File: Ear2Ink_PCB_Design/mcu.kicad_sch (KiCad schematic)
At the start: 44 parts, among them J1 Conn_02x16_Top_Bottom, J2 Conn_01x08_Pin, J3 Conn_01x08_Pin, J4 Micro_SD_Card_Det1, J5 Conn_01x06_Pin, J6 Conn_01x04_Pin, J7 Conn_01x03_Pin, SW1 SW_Push, U1 STM32F411RETx, Y1 MAX7375AXR805

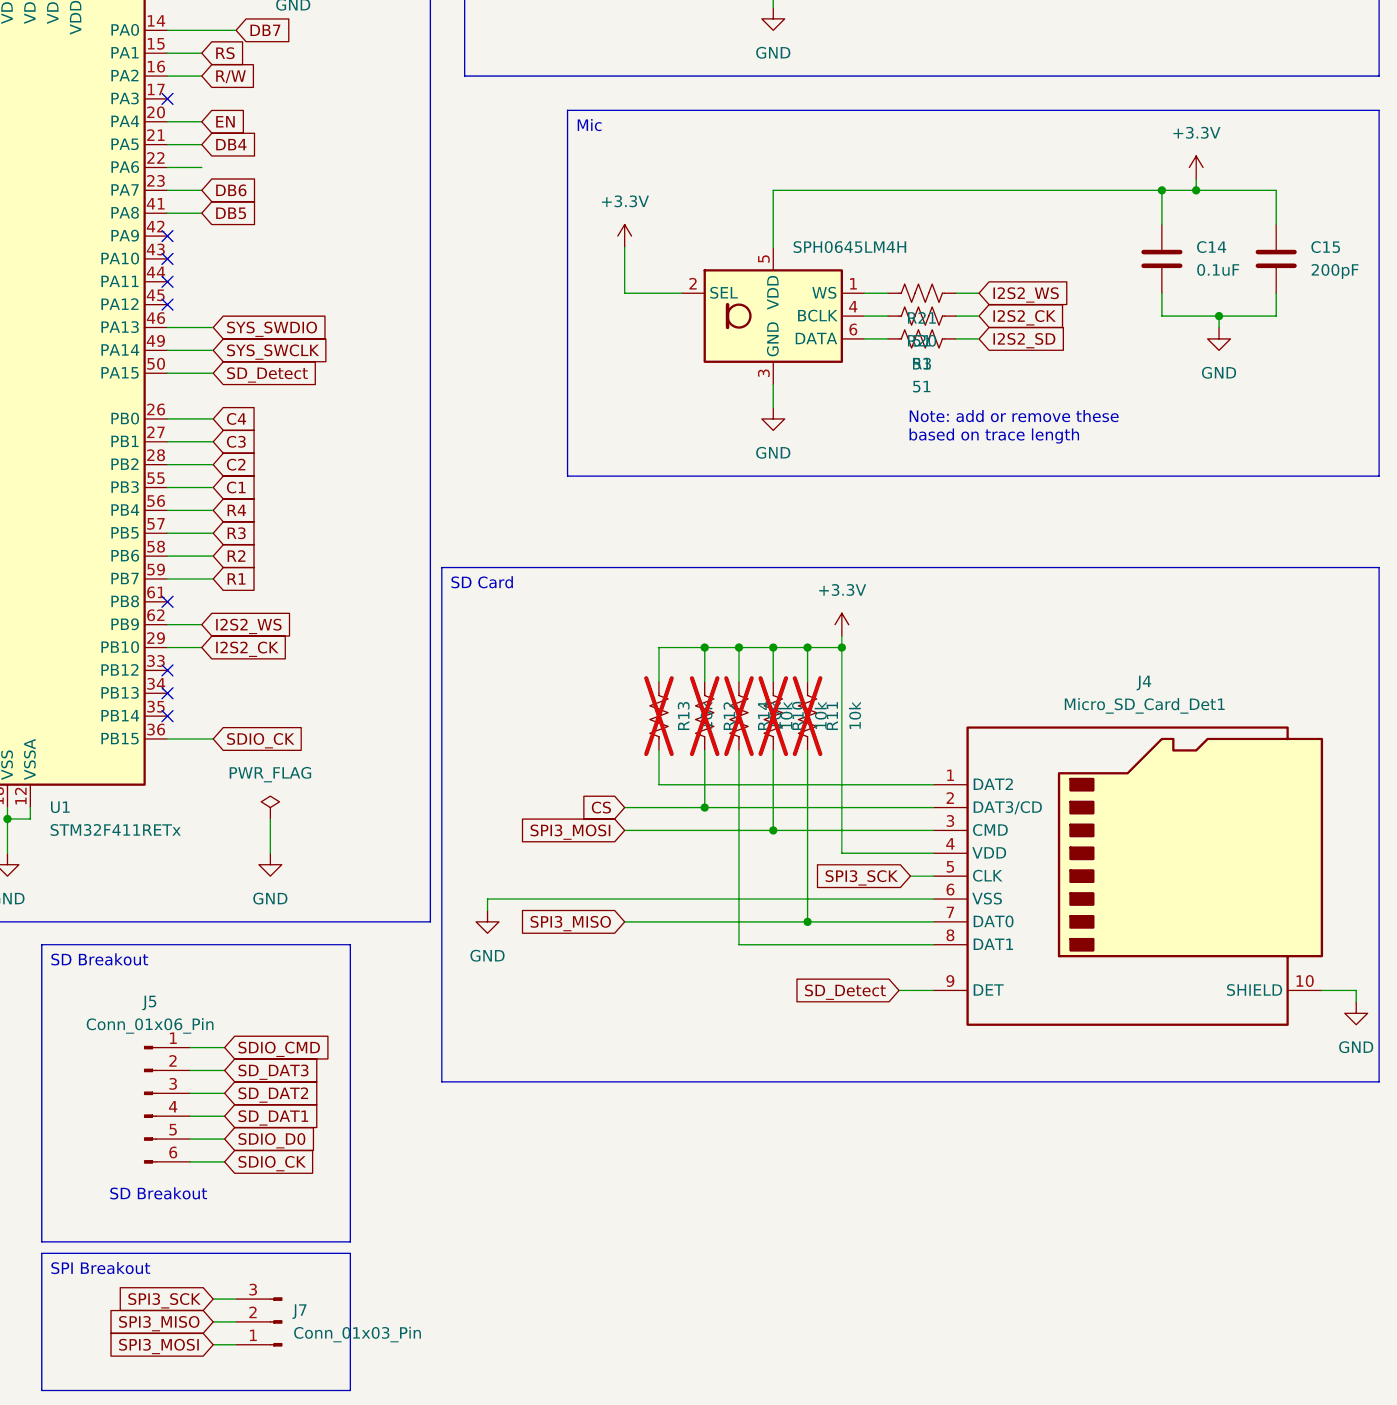
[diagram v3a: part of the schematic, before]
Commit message: fixed footprint issue with SD
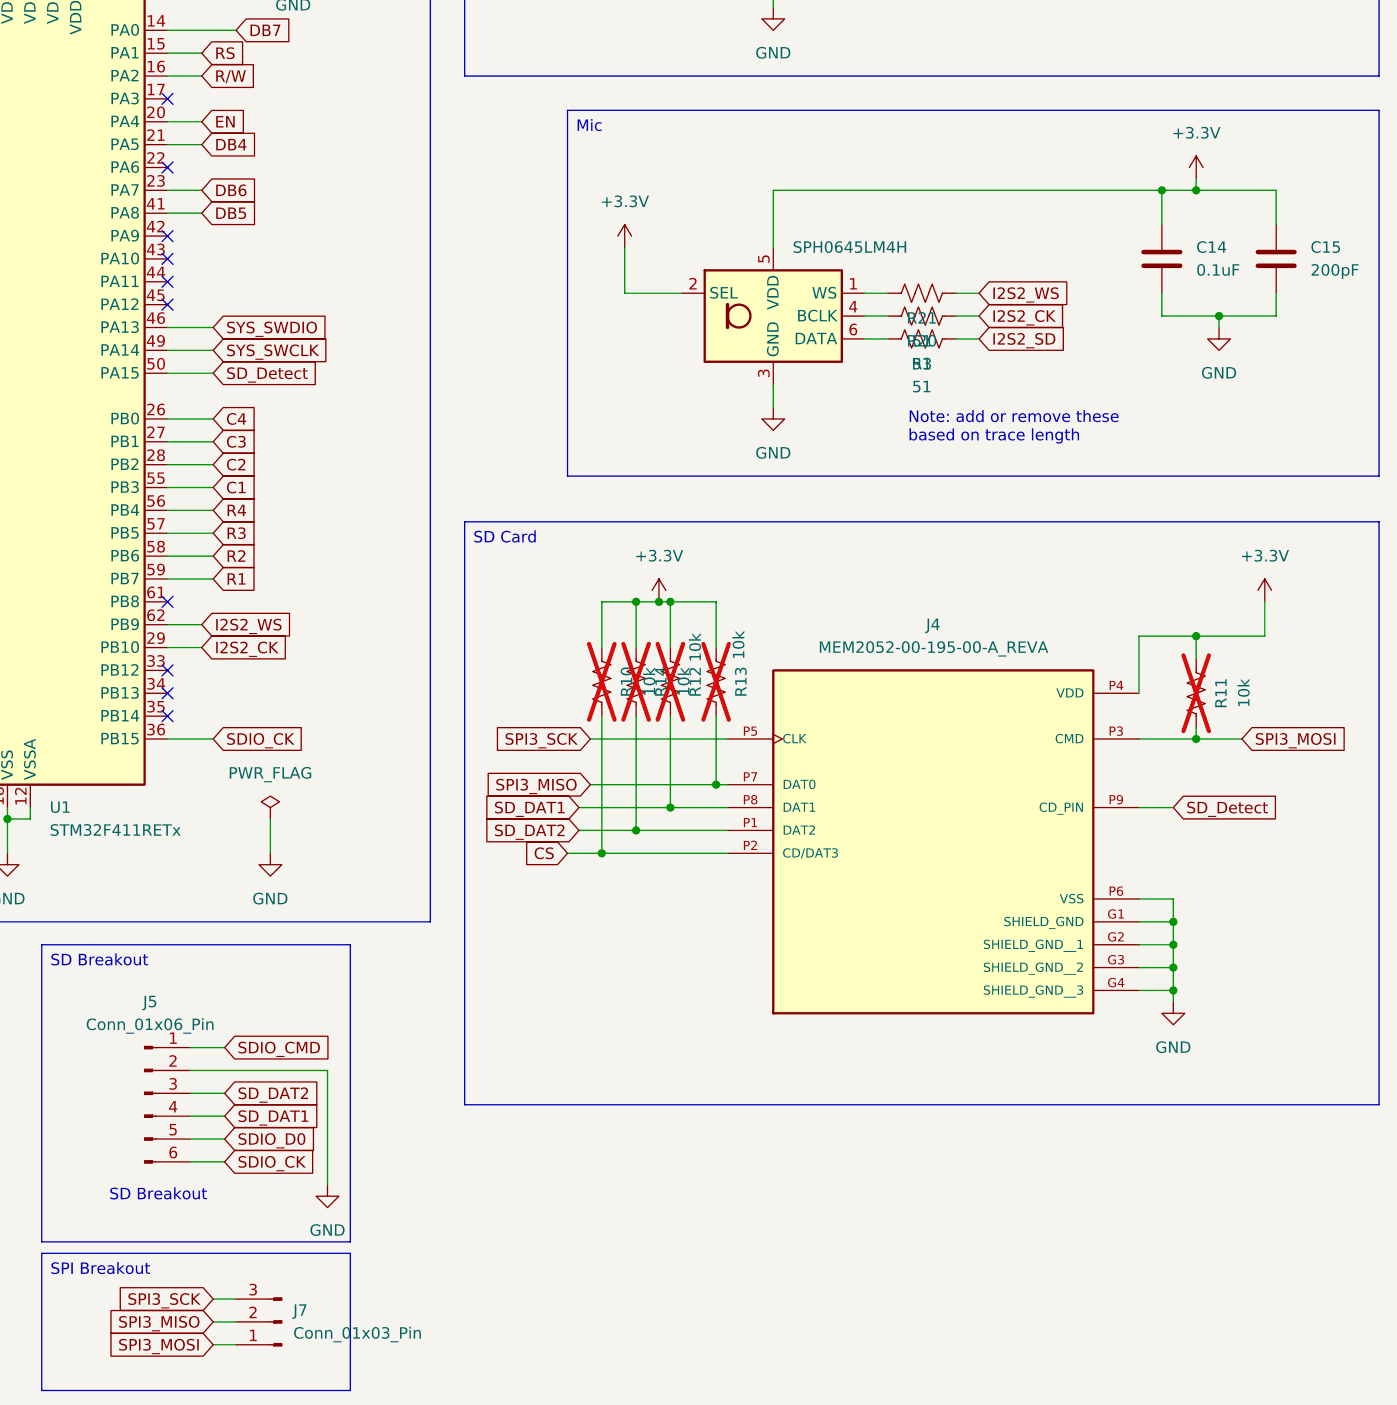
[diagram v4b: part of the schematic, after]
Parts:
- removed J4: Micro_SD_Card_Det1, Connector_Card:SD-SIM_microSD-microSIM_Molex_104168-1620, symbol Connector:Micro_SD_Card_Det1
- added J4: MEM2052-00-195-00-A_REVA, SD Card:GCT_MEM2052-00-195-00-A_REVA, symbol MEM2052-00-195-00-A_REVA:MEM2052-00-195-00-A_REVA
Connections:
- net SD_DAT3 is gone; now on net GND: J5.2 (Pin_2)
- net +3.3V: now also J4.P4 (VDD)
- net CS: now also R10.2, J4.P2 (CD/DAT3); no longer R12.2
- net GND: now also J4.G1 (SHIELD_GND), J4.G2 (SHIELD_GND__1), J4.G3 (SHIELD_GND__2), J4.G4 (SHIELD_GND__3), J4.P6 (VSS)
- net SD_DAT1: now also R12.2, J4.P8 (DAT1)
- net SD_DAT2: now also R14.2, J4.P1 (DAT2)
- net SD_Detect: now also J4.P9 (CD_PIN)
- net SPI3_MISO: now also R13.2, J4.P7 (DAT0); no longer R11.2
- net SPI3_MOSI: now also R11.2, J4.P3 (CMD); no longer R10.2
- net SPI3_SCK: now also J4.P5 (CLK)
- no-connect marks 17 -> 18
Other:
- moved on the sheet: R10, R11, R12, R13, R14

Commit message: some pcb
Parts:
- removed C10: 4.7uF, Capacitor_SMD:C_0603_1608Metric_Pad1.08x0.95mm_HandSolder, symbol Device:C
- removed C7, C8: 0.1uF, Capacitor_SMD:C_0603_1608Metric_Pad1.08x0.95mm_HandSolder, symbol Device:C
- added C21: 4.7uF, Capacitor_SMD:C_0603_1608Metric_Pad1.08x0.95mm_HandSolder, symbol Device:C
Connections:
- net GND: now also C21.2
- net at U1.30 (VCAP1): now also C21.1
- no-connect marks 18 -> 17

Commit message: fixed everything
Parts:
- removed J1: Conn_02x16_Top_Bottom, Connector_PinHeader_2.54mm:PinHeader_2x16_P2.54mm_Vertical, symbol Connector_Generic:Conn_02x16_Top_Bottom
- added J1, J8: Conn_01x16_Pin, Connector_PinHeader_2.54mm:PinHeader_1x16_P2.54mm_Vertical, symbol Connector:Conn_01x16_Pin
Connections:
- net +3.3V: now also J1.15 (Pin_15), J1.2 (Pin_2), J8.2 (Pin_2)
- net DB0: now also J1.7 (Pin_7), J8.7 (Pin_7)
- net DB1: now also J1.8 (Pin_8), J8.8 (Pin_8)
- net DB2: now also J1.9 (Pin_9), J8.9 (Pin_9)
- net DB3: now also J1.10 (Pin_10), J8.10 (Pin_10)
- net DB4: now also J1.11 (Pin_11), J8.11 (Pin_11)
- net DB5: now also J1.12 (Pin_12), J8.12 (Pin_12)
- net DB6: now also J1.13 (Pin_13), J8.13 (Pin_13)
- net DB7: now also J1.14 (Pin_14), J8.14 (Pin_14)
- net EN: now also J1.6 (Pin_6), J8.6 (Pin_6)
- net GND: now also J1.1 (Pin_1), J1.16 (Pin_16), J8.1 (Pin_1)
- net LED+: now also J8.15 (Pin_15)
- net LED-: now also J8.16 (Pin_16)
- net RS: now also J1.4 (Pin_4), J8.4 (Pin_4)
- net R/W: now also J1.5 (Pin_5), J8.5 (Pin_5)
- net SD_DAT1: now also J5.3 (Pin_3); no longer J5.4 (Pin_4)
- net SD_DAT2: now also J5.4 (Pin_4); no longer J5.3 (Pin_3)
- net Vee: now also J1.3 (Pin_3), J8.3 (Pin_3)

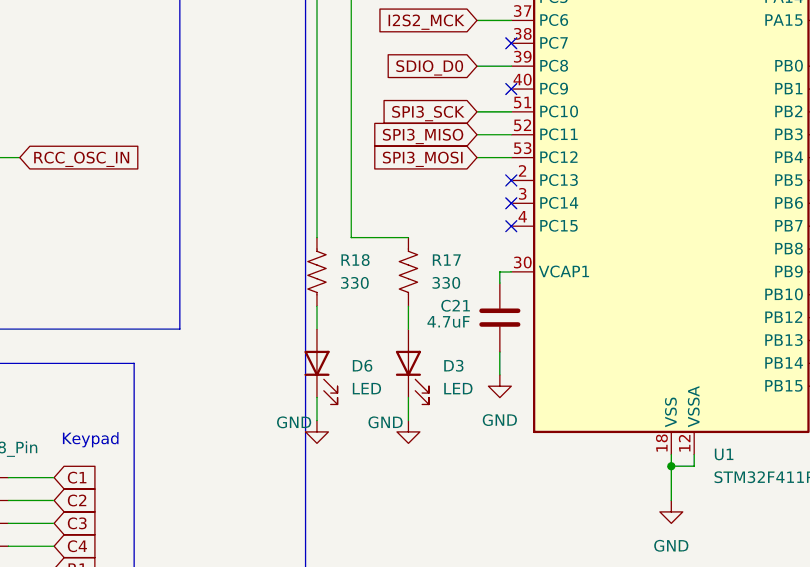
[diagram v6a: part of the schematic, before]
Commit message: resistors changed UPDATE LAYOUT
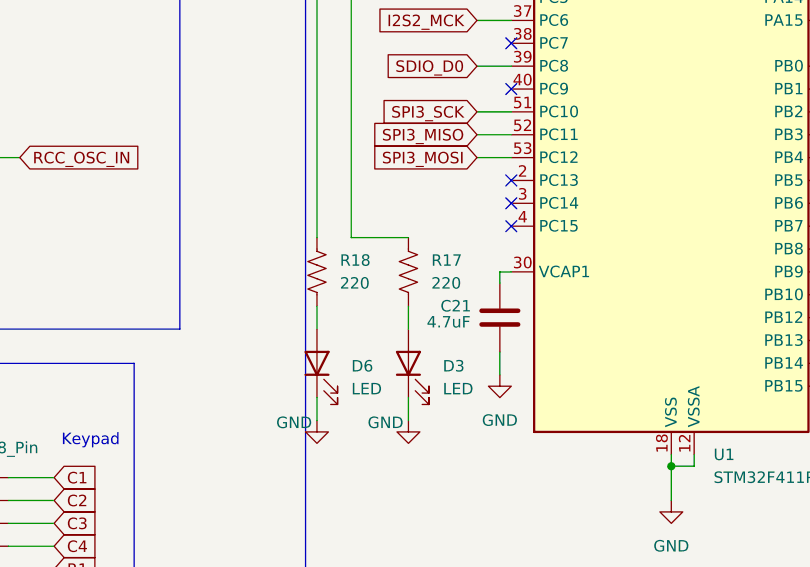
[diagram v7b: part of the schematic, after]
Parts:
- R17, R18: value 330 -> 220
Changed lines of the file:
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@@
 			)
 		)
-		(property "Value" "330"
+		(property "Value" "220"
 			(at 104.14 111.7599 0)
 			(effects
@@
 			)
 		)
-		(property "Value" "330"
+		(property "Value" "220"
 			(at 93.98 111.7599 0)
 			(effects
